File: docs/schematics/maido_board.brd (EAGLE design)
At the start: 100 x 52.1 mm, 40 parts

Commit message: Initial Layout
Schematic completely wired. Have initial placement (no routing)
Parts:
- removed LED3, LED4: (no value), SparkFun-LED:LED5MM
- removed R11: 10kOhm, adafruit:R0805
- removed TP2, TP3, TP4: TEST-POINT3X5, SparkFun-Passives:PAD.03X.05
- R1, R2, R3, R4: value 300ohm -> 330
- R10, R5, R6, R7, R8, R9: value 10kOhm -> 10k
- U$3: device nate_parts:ELECTRIC_IMP_BREAKOUT -> nate_parts:ELECTRIC_IMP_BREAKOUT@1
- moved JP1 308.1 mm to (90.2, 17.8)
- moved U$10 290.8 mm to (97.8, 35.6)
- moved U$12 277.1 mm to (97.8, 3.81)
- moved TP1 275.1 mm to (47.6, 8.89)
- moved LED2 252.0 mm to (25.4, 24.1)
- moved U$6 250.4 mm to (68.6, 27.9)
- moved U$9 239.2 mm to (38.1, 27.9)
- moved LED1 237.1 mm to (10.2, 24.1)
- moved U$5 234.0 mm to (68.6, 6.35)
- moved U$7 225.1 mm to (3.81, 47.0)
- moved U$8 220.1 mm to (38.1, 6.35)
- moved U$11 205.5 mm to (3.81, 2.54)
- moved R9 205.4 mm to (31.8, 41.9), flipped to the bottom
- moved R8 196.6 mm to (26.7, 41.9), flipped to the bottom
- moved R10 194.9 mm to (10.2, 41.9), flipped to the bottom
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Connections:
- net N$1 renamed OLED_DATA
- net N$2 renamed OLED_CLK
- net N$3 renamed OLED_DC
- net N$4 renamed OLED_CS
- net N$5 renamed OLED_RST
- net N$7 renamed IMP_RX
- removed net N$6: U$1.2
- removed net SPK: SP1.P$2, U$1.6
- new net BIG_LED: R2.1, U$1.11
- new net IMP_TX: U$1.2, U$3.6
- new net LED1: LED1.A, U$1.7
- new net LED2: LED2.A, U$1.10
- new net N$1: LSW1.LEDA, R1.2
- new net N$2: LSW2.LEDA, R2.2
- new net N$3: LED1.K, R3.1
- new net N$4: LED2.K, R4.1
- new net SPEAKER: SP1.P$2, U$1.9
- new net SW1: R10.1, SW1.16, U$1.17
- new net SW2: SW1.15, U$3.8
- new net SW4: SW1.13, U$3.4
- new net SW5: R7.1, SW1.12, U$1.18
- new net SW6: R8.1, SW1.11, U$1.19
- new net SW7: R9.1, SW1.10, U$1.20
- new net TP1: TP1.P$1, U$3.9
- new net TRIG2: LSW2.SWA2, R6.1, U$1.6
- new net TRIGGER: LSW1.SWA2, R5.1, U$1.5
- new net WIFI: LSW1.LEDC, U$1.8, U$3.5
- net GND: now also JP1.1, LSW2.LEDC, R10.2, R3.2, R4.2, R5.2, R6.2, R7.2, R8.2, R9.2, U$3.1, U$3.12, U$4.1
- net VCC: now also JP1.2, LSW1.SWA1, LSW2.SWA1, R1.1, SW1.1, SW1.2, SW1.4, SW1.5, SW1.6, SW1.7, U$3.2, U$4.2
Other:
- board size 100 x 52.1 mm -> 101.6 x 50.8 mm

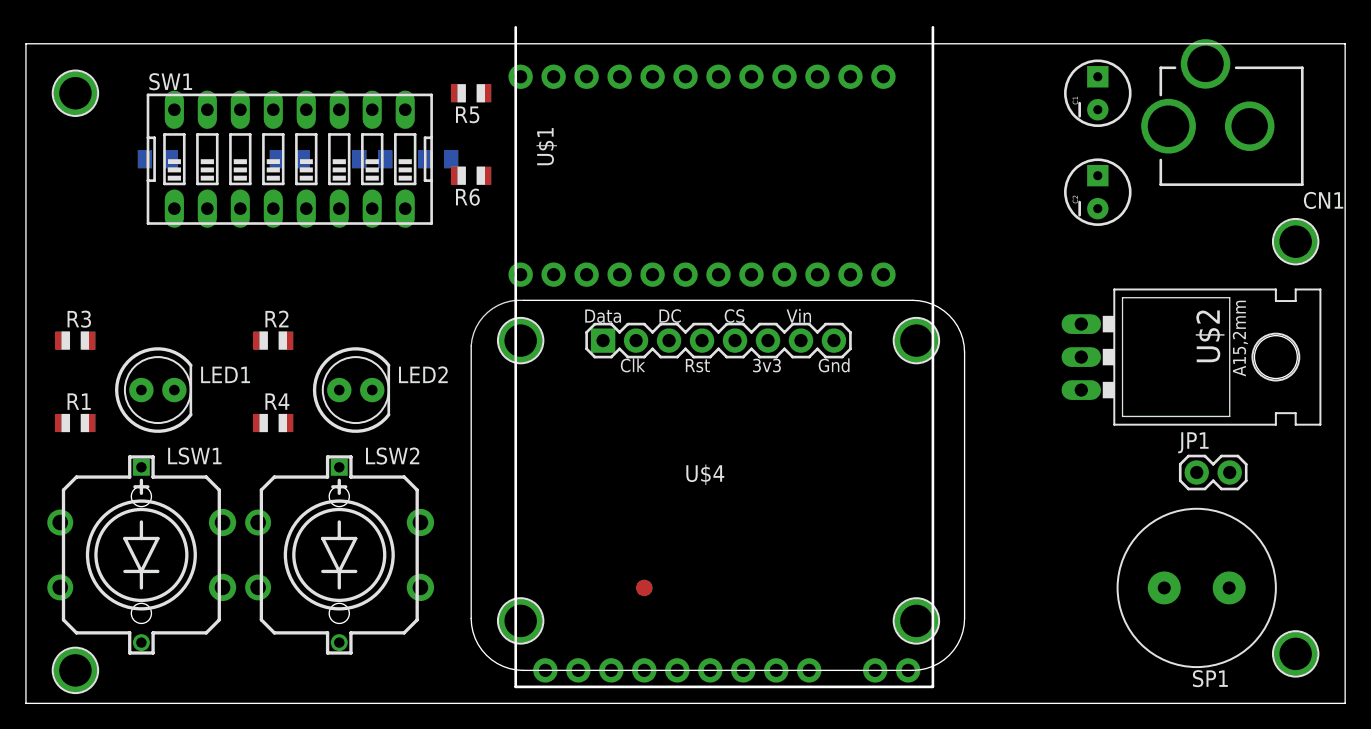
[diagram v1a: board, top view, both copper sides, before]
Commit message: Fixed pinout on OLED
Oops! That would have been a horrible mistake. I also messed around with
routing some.
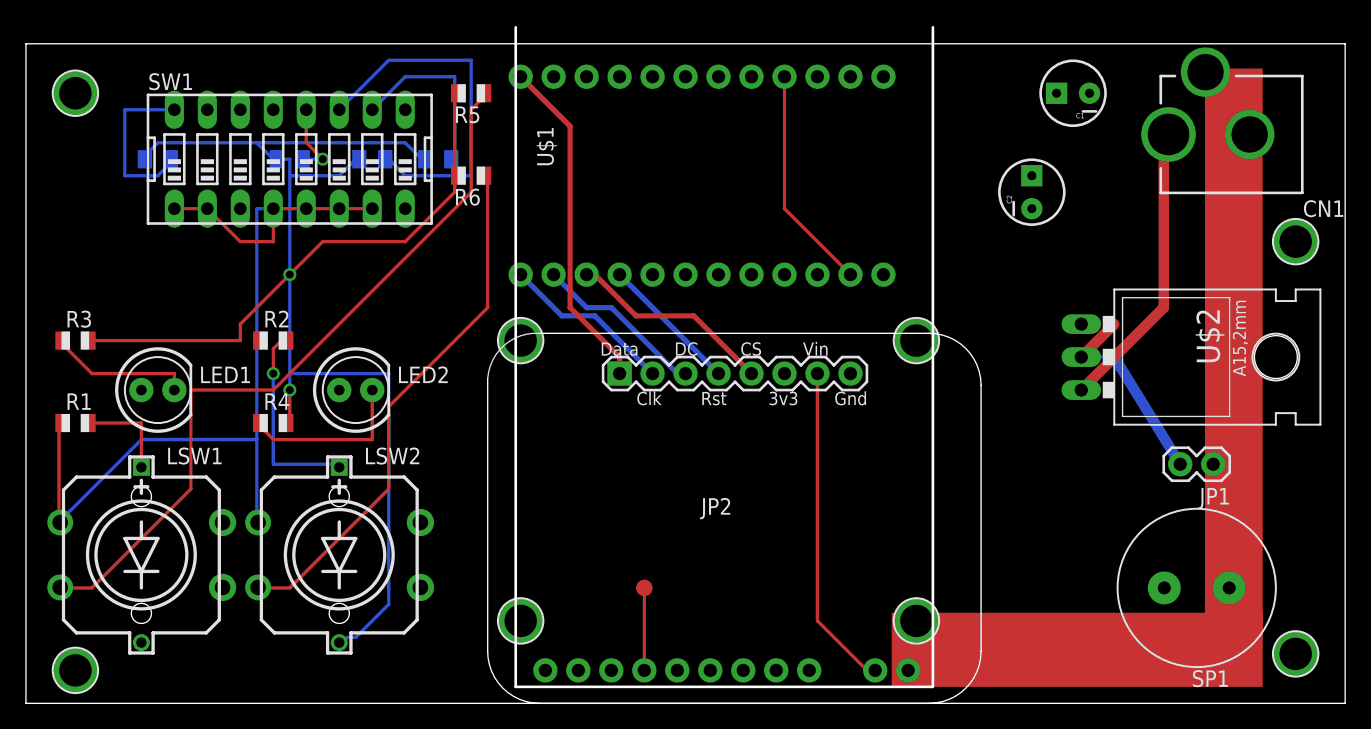
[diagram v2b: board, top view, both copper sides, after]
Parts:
- removed U$4: OLED_DISPLAY, nate_parts:OLED_128X64
- added JP2: (no value), nate_parts:OLED_128X64
- moved C2 5.08 mm to (77.5, 39.4)
- moved C1 1.91 mm to (80.6, 47.0), turned to 180 degrees
- moved JP1 1.42 mm to (91.4, 18.4), turned to 180 degrees
- moved CN1 0.64 mm to (101.6, 43.8)
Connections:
- net GND: now also JP2.8; no longer U$4.1
- net OLED_CLK: now also JP2.2; no longer U$4.7
- net OLED_CS: now also JP2.5; no longer U$4.4
- net OLED_DATA: now also JP2.1; no longer U$4.8
- net OLED_DC: now also JP2.3; no longer U$4.6
- net OLED_RST: now also JP2.4; no longer U$4.5
- net VCC: now also JP2.7; no longer U$4.2
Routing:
- net GND: track 0.00 -> 188.3 mm, vias 0 -> 2
- net VCC: track 0.00 -> 111.2 mm
- net TRIGGER: track 0.00 -> 57.4 mm
- net TRIG2: track 0.00 -> 41.0 mm
- net SW6: track 0.00 -> 27.8 mm
- net OLED_DATA: track 0.00 -> 26.0 mm
- net VIN: track 0.00 -> 24.4 mm
- net OLED_CS: track 0.00 -> 15.9 mm
- net N$2: track 0.00 -> 15.5 mm, vias 0 -> 1
- net SW7: track 0.00 -> 14.0 mm
- net N$4: track 0.00 -> 13.5 mm
- net SW1: track 0.00 -> 13.5 mm
- net OLED_DC: track 0.00 -> 13.3 mm
- net OLED_CLK: track 0.00 -> 13.3 mm
- net N$3: track 0.00 -> 11.5 mm
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
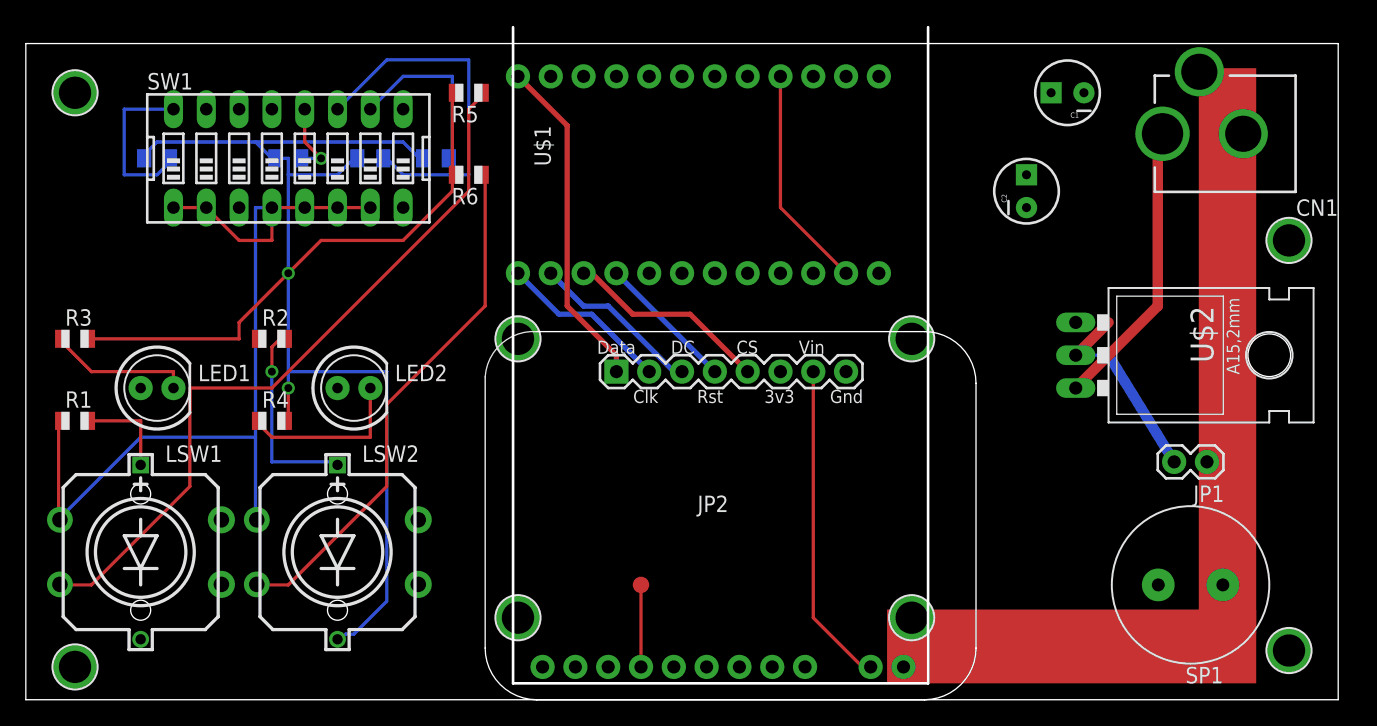
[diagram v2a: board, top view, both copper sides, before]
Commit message: Layout Work
More work on the layout. I pretty carefully managed power to from the DC
header to the VREG to the Imp (by FAR the biggest power consumer on the
board). I also rearranged some parts to try to optimize placement. Next
up- auto route.
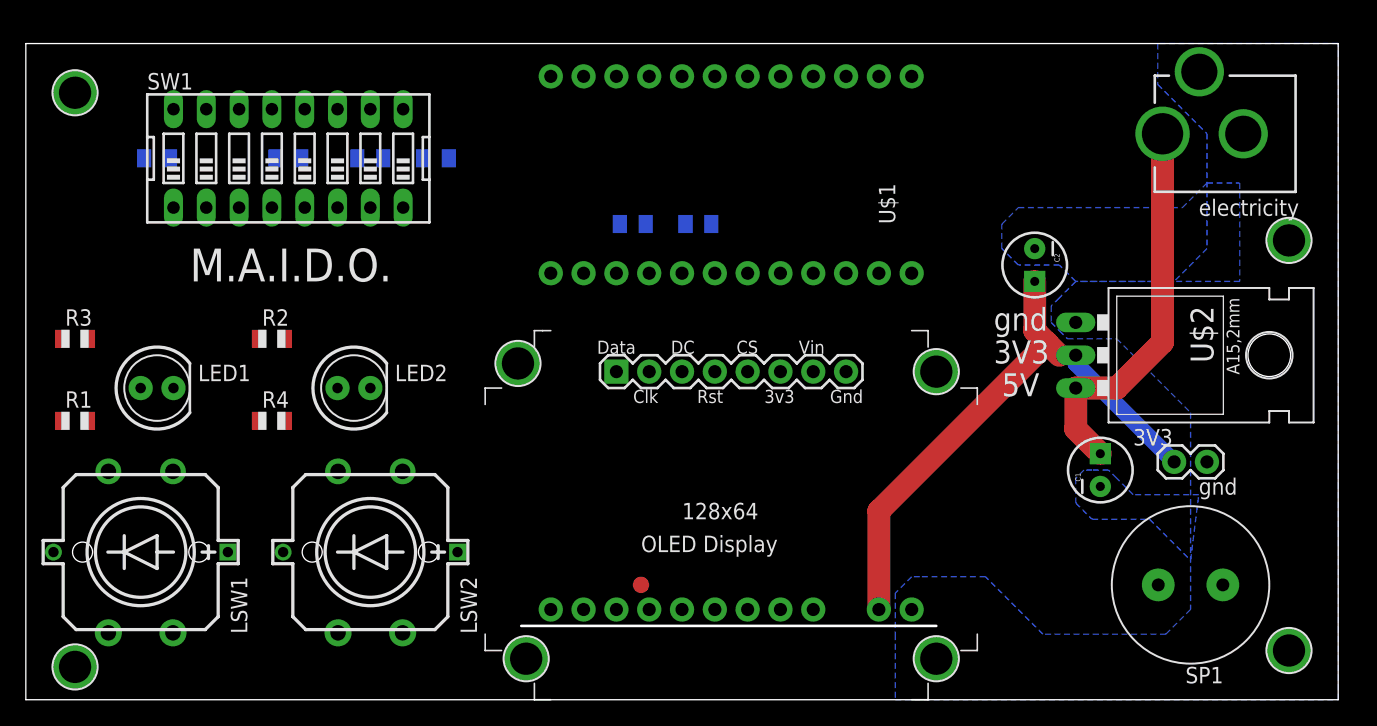
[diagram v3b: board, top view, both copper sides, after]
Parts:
- U$2: value V_REG_LD1117VXX -> VREG
- U$3: device nate_parts:ELECTRIC_IMP_BREAKOUT@1 -> nate_parts:ELECTRIC_IMP_BREAKOUT
- moved C1 29.3 mm to (83.2, 17.8), turned to 90 degrees
- moved R6 18.2 mm to (52.1, 36.8), flipped to the bottom, turned to 0 degrees
- moved R5 16.3 mm to (47.0, 36.8), flipped to the bottom, turned to 0 degrees
- moved C2 5.75 mm to (78.1, 33.7), turned to 270 degrees
- moved U$3 4.49 mm to (70.5, 5.71)
- moved U$5 3.70 mm to (70.5, 3.17)
- moved U$8 3.24 mm to (38.7, 3.17)
- moved U$6 3.18 mm to (70.5, 25.4)
- moved LSW2 2.54 mm to (26.7, 11.4), turned to 180 degrees
- moved U$9 1.91 mm to (38.1, 26.0)
- turned LSW1 to 180 degrees
- turned U$1 to 90 degrees
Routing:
- net GND: track 188.3 -> 0.00 mm, vias 2 -> 0
- net VCC: track 111.2 -> 45.2 mm
- net TRIGGER: track 57.4 -> 0.00 mm
- net TRIG2: track 41.0 -> 0.00 mm
- net SW6: track 27.8 -> 0.00 mm
- net OLED_DATA: track 26.0 -> 0.00 mm
- net OLED_CS: track 15.9 -> 0.00 mm
- net N$2: track 15.5 -> 0.00 mm, vias 1 -> 0
- net SW7: track 14.0 -> 0.00 mm
- net N$4: track 13.5 -> 0.00 mm
- net SW1: track 13.5 -> 0.00 mm
- net OLED_DC: track 13.3 -> 0.00 mm
- net OLED_CLK: track 13.3 -> 0.00 mm
- net N$3: track 11.5 -> 0.00 mm
- net OLED_RST: track 10.8 -> 0.00 mm
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- added copper zone on layer 16, net GND
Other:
- board text added: "3V3"
- board text added: "5V"
- board text added: "M.A.I.D.O."
- board text added: "electricity"
- board text added: "gnd"

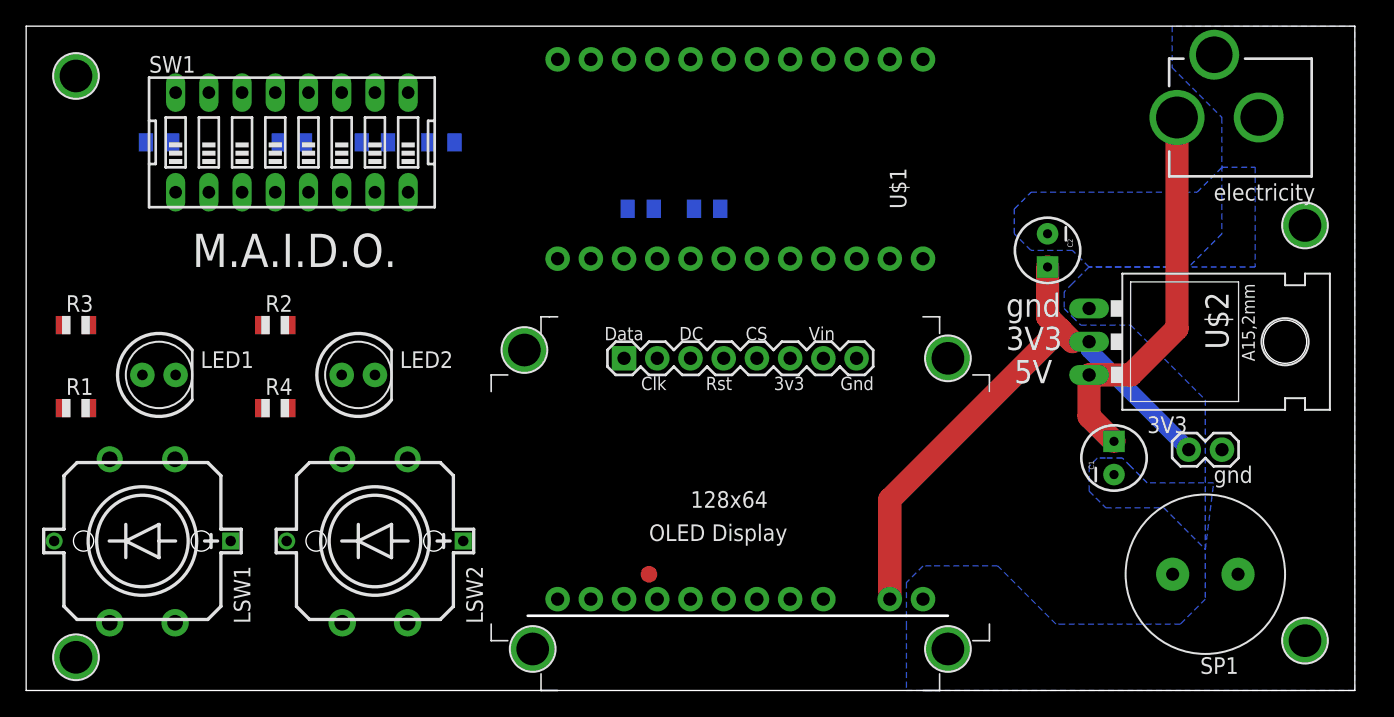
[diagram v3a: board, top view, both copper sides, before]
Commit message: Final Built Board
Final built board schematic + layout (received board already, tested,
works). Added IO pins to the arduino code, works.
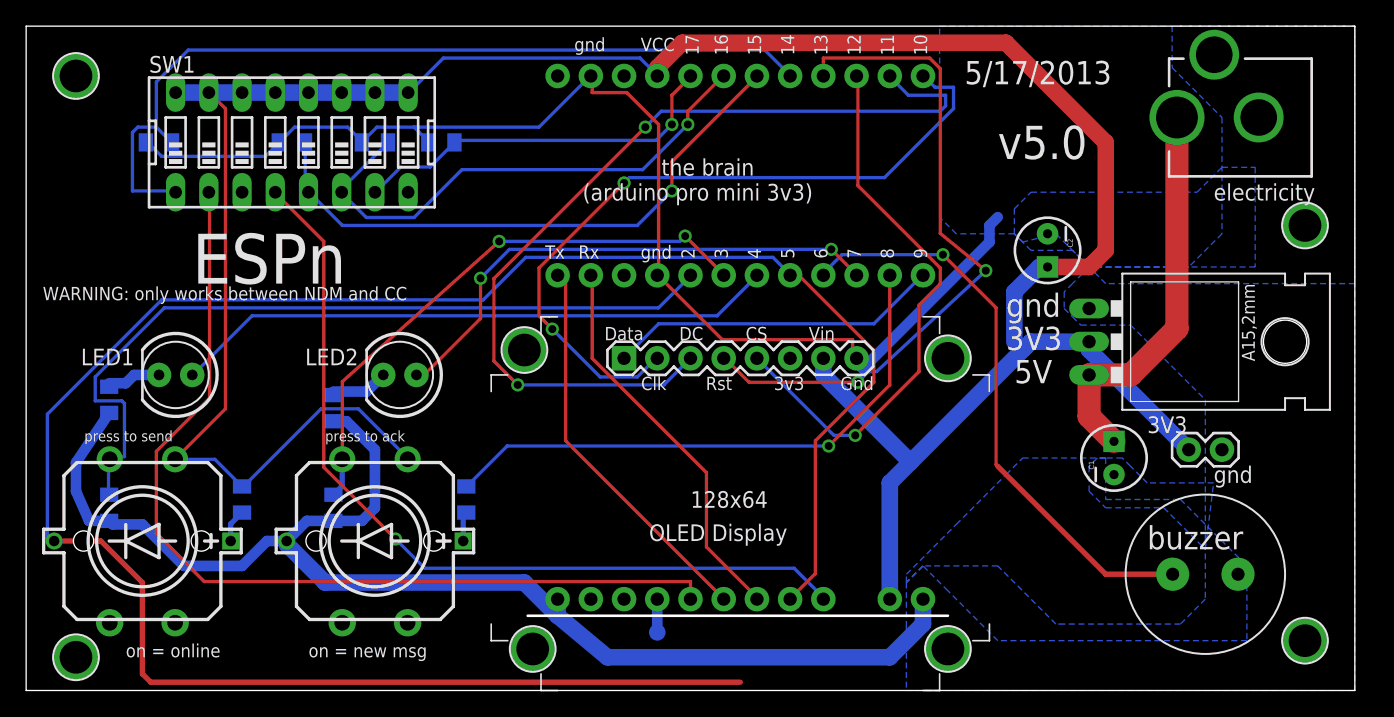
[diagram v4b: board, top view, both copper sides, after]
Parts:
- moved R5 46.6 mm to (6.35, 14.0), turned to 270 degrees
- moved R6 36.6 mm to (23.5, 14.0), turned to 270 degrees
- moved R2 19.8 mm to (33.7, 14.6), flipped to the bottom, turned to 270 degrees
- moved R1 14.5 mm to (16.5, 14.6), flipped to the bottom, turned to 270 degrees
- moved R3 6.25 mm to (6.35, 22.2), flipped to the bottom, turned to 270 degrees
- moved TP1 4.49 mm to (48.3, 4.45), flipped to the bottom
- moved R4 4.45 mm to (23.5, 21.6), flipped to the bottom, turned to 270 degrees
- moved LED2 3.18 mm to (28.6, 24.1), turned to 180 degrees
- moved U$1 1.27 mm to (53.3, 39.4)
- moved LED1 1.27 mm to (11.4, 24.1), turned to 180 degrees
- renumbered LSW1 to SEND, LSW2 to ACK
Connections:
- net SW1: now also SW1.1; no longer SW1.16
- net SW2: now also SW1.2; no longer SW1.15
- net SW4: now also SW1.4; no longer SW1.13
- net SW5: now also SW1.5; no longer SW1.12
- net SW6: now also SW1.6; no longer SW1.11
- net SW7: now also SW1.7; no longer SW1.10
- net VCC: now also SW1.10, SW1.11, SW1.12, SW1.13, SW1.14, SW1.15, SW1.16, SW1.9; no longer SW1.1, SW1.2, SW1.4, SW1.5, SW1.6, SW1.7
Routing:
- net GND: track 0.00 -> 193.1 mm
- net WIFI: track 0.00 -> 164.0 mm
- net VCC: track 45.2 -> 202.3 mm
- net SW2: track 0.00 -> 71.5 mm
- net OLED_DC: track 0.00 -> 68.7 mm, vias 0 -> 2
- net SW1: track 0.00 -> 65.3 mm
- net SW4: track 0.00 -> 65.0 mm, vias 0 -> 1
- net TRIGGER: track 0.00 -> 61.0 mm
- net OLED_CLK: track 0.00 -> 56.3 mm, vias 0 -> 2
- net OLED_RST: track 0.00 -> 51.9 mm, vias 0 -> 2
- net LED1: track 0.00 -> 46.4 mm
- net SW5: track 0.00 -> 45.4 mm, vias 0 -> 1
- net SPEAKER: track 0.00 -> 44.6 mm, vias 0 -> 1
- net BIG_LED: track 0.00 -> 44.0 mm, vias 0 -> 1
- net TRIG2: track 0.00 -> 43.6 mm, vias 0 -> 2
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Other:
- board text added: "(arduino pro mini 3v3)"
- board text added: "10"
- board text added: "11"
- board text added: "12"
- board text added: "13"
- board text added: "14"
- board text added: "15"
- board text added: "16"
- board text added: "17"
- board text added: "2"
- board text added: "3"
- board text added: "4"
- board text added: "5"
- board text added: "5/17/2013"
- board text added: "6"
- board text added: "7"
- board text added: "8"
- board text added: "9"
- board text added: "<3"
- board text added: "ESPn"
- board text added: "Rx"
- board text added: "Tx"
- board text added: "VCC"
- board text added: "WARNING: only works between NDM and CC"
- board text added: "buzzer"
- board text added: "created with love for my chanchan"
- board text added: "love you!"
- board text added: "on = new msg"
- board text added: "on = online"
- board text added: "press to ack"
- board text added: "press to send"
- board text added: "the brain"
- board text added: "v5.0"
- board text removed: "M.A.I.D.O."
